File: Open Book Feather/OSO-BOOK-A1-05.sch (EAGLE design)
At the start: 129 parts, among them J1 SJ-43514-SMT, J2 10118193-0001LF, Q1 DMG341, Q2 IRLML0100, SW1 SPDT_SWITCH, U1 AP2112-3.3, U2 MCP73831T-2ACI/OT, U3 ATSAMD51J64-TQFP(10X10), U4 GD25Q16C (or GD25Q32C), U5 74AC165D, U6 GD25Q16C (or GD25Q32C), U7 MAX4468EKAT, X1 JSTPH, X2 2x5 0.05" SWD

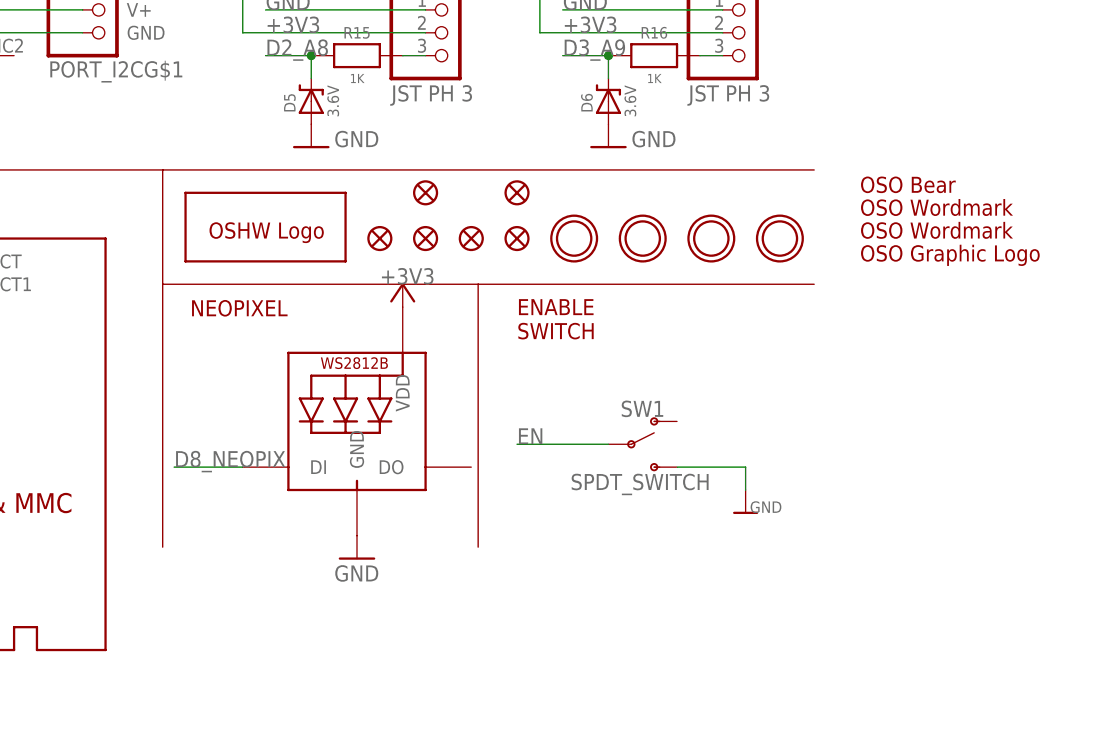
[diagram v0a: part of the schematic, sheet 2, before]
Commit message: right angle neopixel near reset button
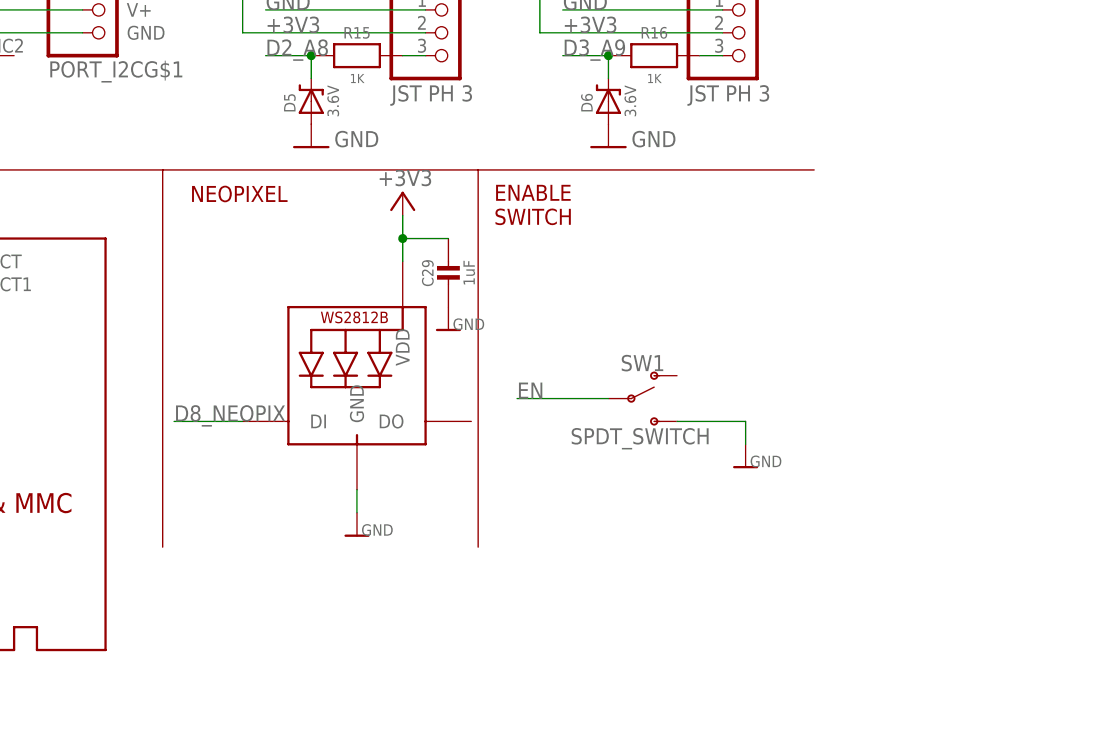
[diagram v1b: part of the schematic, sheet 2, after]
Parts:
- removed STATUS: WS2812B3535, adafruit:WS2812B3535
- added C36: 4.5nF, microbuilder:CAP_CERAMIC0805-NOOUTLINE
- added NEOPIX: WS2812B_4020, microbuilder:WS2812B_4020
- C29: value 4.5nF -> 1uF
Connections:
- net +3V3: now also C29.1, NEOPIX.VDD; no longer STATUS.VDD
- net D8_NEOPIX: now also NEOPIX.DI; no longer STATUS.DI
- net GND: now also C36.2, NEOPIX.GND; no longer STATUS.GND
- net SHIELD: now also C36.1; no longer C29.1
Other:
- moved on the sheet: SW1

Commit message: extend inductor's pad out from underneath
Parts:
- L1: device microbuilder:INDUCTORNR401 -> Adafruit 3.5in 480x320 FeatherWing:MICROBUILDER_INDUCTORNR401_BIGPADS
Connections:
- net +3V3: now also L1.1; no longer L1.2
- net N$3: now also L1.2; no longer L1.1
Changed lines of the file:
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@@
 <part name="C24" library="microbuilder" deviceset="CAP_CERAMIC" device="0805-NOOUTLINE" value="4.7uF/25V"/>
 <part name="D4" library="microbuilder" deviceset="DIODE-SCHOTTKY" device="SOD-123" value="MBR0530"/>
-<part name="L1" library="microbuilder" deviceset="INDUCTOR" device="NR401" value="10uH"/>
 <part name="R12" library="microbuilder" deviceset="RESISTOR" device="0805_10MGAP" value="0.47ohm"/>
 <part name="U$10" library="microbuilder" deviceset="GND" device=""/>
@@
 <part name="C29" library="microbuilder" deviceset="CAP_CERAMIC" device="0805-NOOUTLINE" value="1uF"/>
 <part name="U$46" library="microbuilder" deviceset="GND" device=""/>
+<part name="L1" library="Adafruit 3.5in 480x320 FeatherWing" deviceset="MICROBUILDER_INDUCTOR" device="NR401_BIGPADS" value="10uH"/>
 </parts>
 <sheets>
@@
 <attribute name="VALUE" x="104.1" y="144.78" size="1.27" layer="96" rot="MR270" align="center"/>
 </instance>
-<instance part="L1" gate="G$1" x="83.82" y="149.86" smashed="yes" rot="MR0">
-<attribute name="NAME" x="83.82" y="152.4" size="1.27" layer="95" rot="MR0" align="center"/>
-<attribute name="VALUE" x="83.82" y="148.32" size="1.27" layer="96" rot="MR0" align="center"/>
-</instance>
 <instance part="R12" gate="G$1" x="91.44" y="121.92" smashed="yes" rot="MR270">
 <attribute name="NAME" x="88.9" y="121.92" size="1.27" layer="95" font="vector" rot="MR270" align="center"/>
@@
 <instance part="U$46" gate="G$1" x="215.9" y="48.26" smashed="yes" rot="MR0">
 <attribute name="VALUE" x="219.964" y="48.26" size="1.27" layer="96" rot="MR0"/>
+</instance>
+<instance part="L1" gate="G$1" x="83.82" y="149.86" smashed="yes">
+<attribute name="NAME" x="83.82" y="152.4" size="1.27" layer="95" align="center"/>
+<attribute name="VALUE" x="83.82" y="148.32" size="1.27" layer="96" align="center"/>
 </instance>
 </instances>
@@
 <net name="+3V3" class="1">
 <segment>
-<pinref part="L1" gate="G$1" pin="2"/>
 <wire x1="76.2" y1="154.94" x2="76.2" y2="149.86" width="0.1524" layer="91"/>
 <wire x1="76.2" y1="149.86" x2="78.74" y2="149.86" width="0.1524" layer="91"/>
 <pinref part="+3V7" gate="G$1" pin="+3V3"/>
+<pinref part="L1" gate="G$1" pin="1"/>
 </segment>
 <segment>
@@
 <wire x1="91.44" y1="149.86" x2="101.6" y2="149.86" width="0.1524" layer="91"/>
 <wire x1="101.6" y1="149.86" x2="101.6" y2="147.32" width="0.1524" layer="91"/>
-<pinref part="L1" gate="G$1" pin="1"/>
 <wire x1="91.44" y1="149.86" x2="88.9" y2="149.86" width="0.1524" layer="91"/>
 <junction x="91.44" y="149.86"/>
@@
 <pinref part="C24" gate="G$1" pin="1"/>
 <wire x1="114.3" y1="149.86" x2="114.3" y2="144.78" width="0.1524" layer="91"/>
-</segment>
-</net>
+<pinref part="L1" gate="G$1" pin="2"/>
+</segment>
+</net>

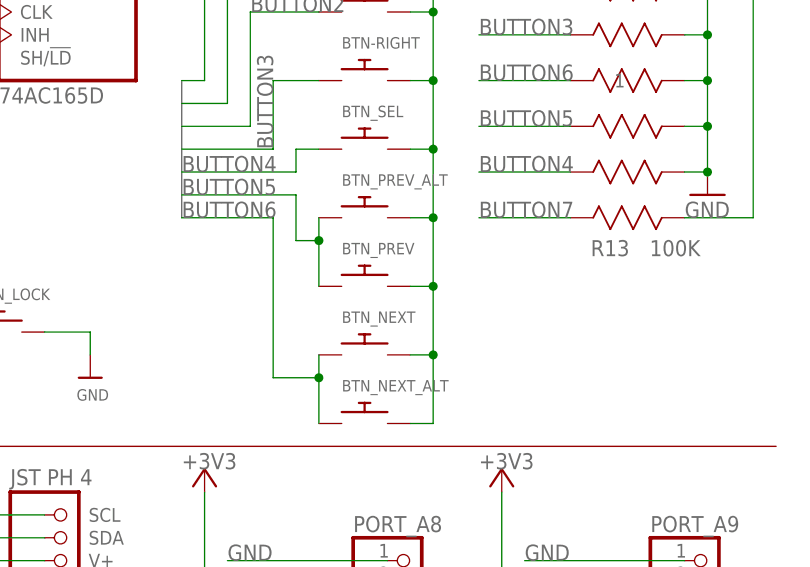
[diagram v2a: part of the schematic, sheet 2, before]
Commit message: DNP side buttons
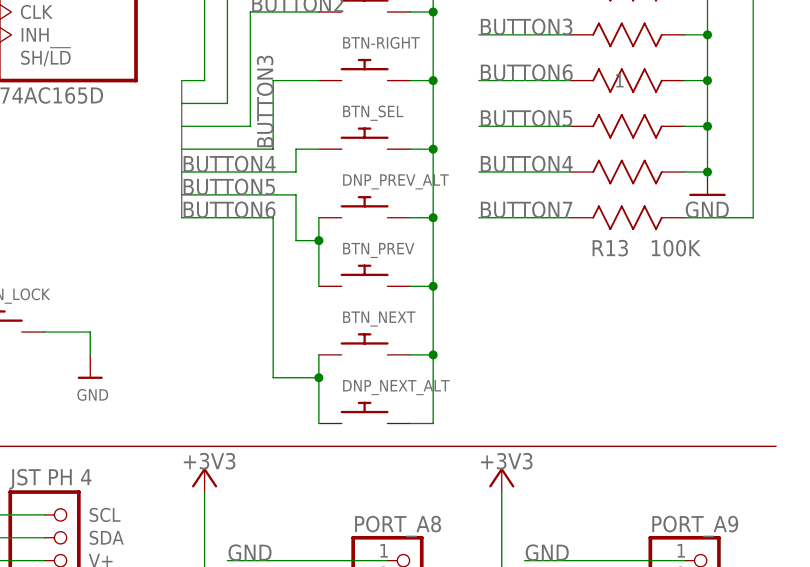
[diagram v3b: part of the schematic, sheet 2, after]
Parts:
- renumbered BTN_NEXT_ALT to DNP_NEXT_ALT, BTN_PREV_ALT to DNP_PREV_ALT

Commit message: last tweaks to A1-05 before sending to fab
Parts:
- removed U$44: OSO_GRAPHIC, My Stuff:OSO_GRAPHIC
- removed U$45: OSO_BEAR, My Stuff:OSO_BEAR
- removed U$47: OSO_TEXT, My Stuff:OSO_TEXT
- removed U$48: OSO_TEXTOSO_TEXT_ONELINE_125MIL, My Stuff:OSO_TEXTOSO_TEXT_ONELINE_125MIL
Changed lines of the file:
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@@
 <part name="GND7" library="supply1" deviceset="GND" device=""/>
 <part name="C10" library="microbuilder" deviceset="CAP_CERAMIC" device="0805_10MGAP" value="1uF"/>
-<part name="U$44" library="My Stuff" deviceset="OSO_GRAPHIC" device=""/>
-<part name="U$45" library="My Stuff" deviceset="OSO_BEAR" device=""/>
-<part name="U$47" library="My Stuff" deviceset="OSO_TEXT" device=""/>
-<part name="U$48" library="My Stuff" deviceset="OSO_TEXT" device="OSO_TEXT_ONELINE_125MIL"/>
 <part name="LED" library="adafruit" deviceset="LED" device="CHIP-LED0805" value="RED"/>
 <part name="CHG" library="adafruit" deviceset="LED" device="CHIP-LED0805" value="AMBER"/>
@@
 <instance part="FID5" gate="G$1" x="111.76" y="15.24" smashed="yes"/>
 <instance part="FID6" gate="G$1" x="121.92" y="15.24" smashed="yes"/>
-<instance part="U$44" gate="G$1" x="160.02" y="7.62" smashed="yes"/>
-<instance part="U$45" gate="G$1" x="160.02" y="15.24" smashed="yes"/>
-<instance part="U$47" gate="G$1" x="160.02" y="10.16" smashed="yes"/>
-<instance part="U$48" gate="G$1" x="160.02" y="12.7" smashed="yes"/>
 </instances>
 <busses>

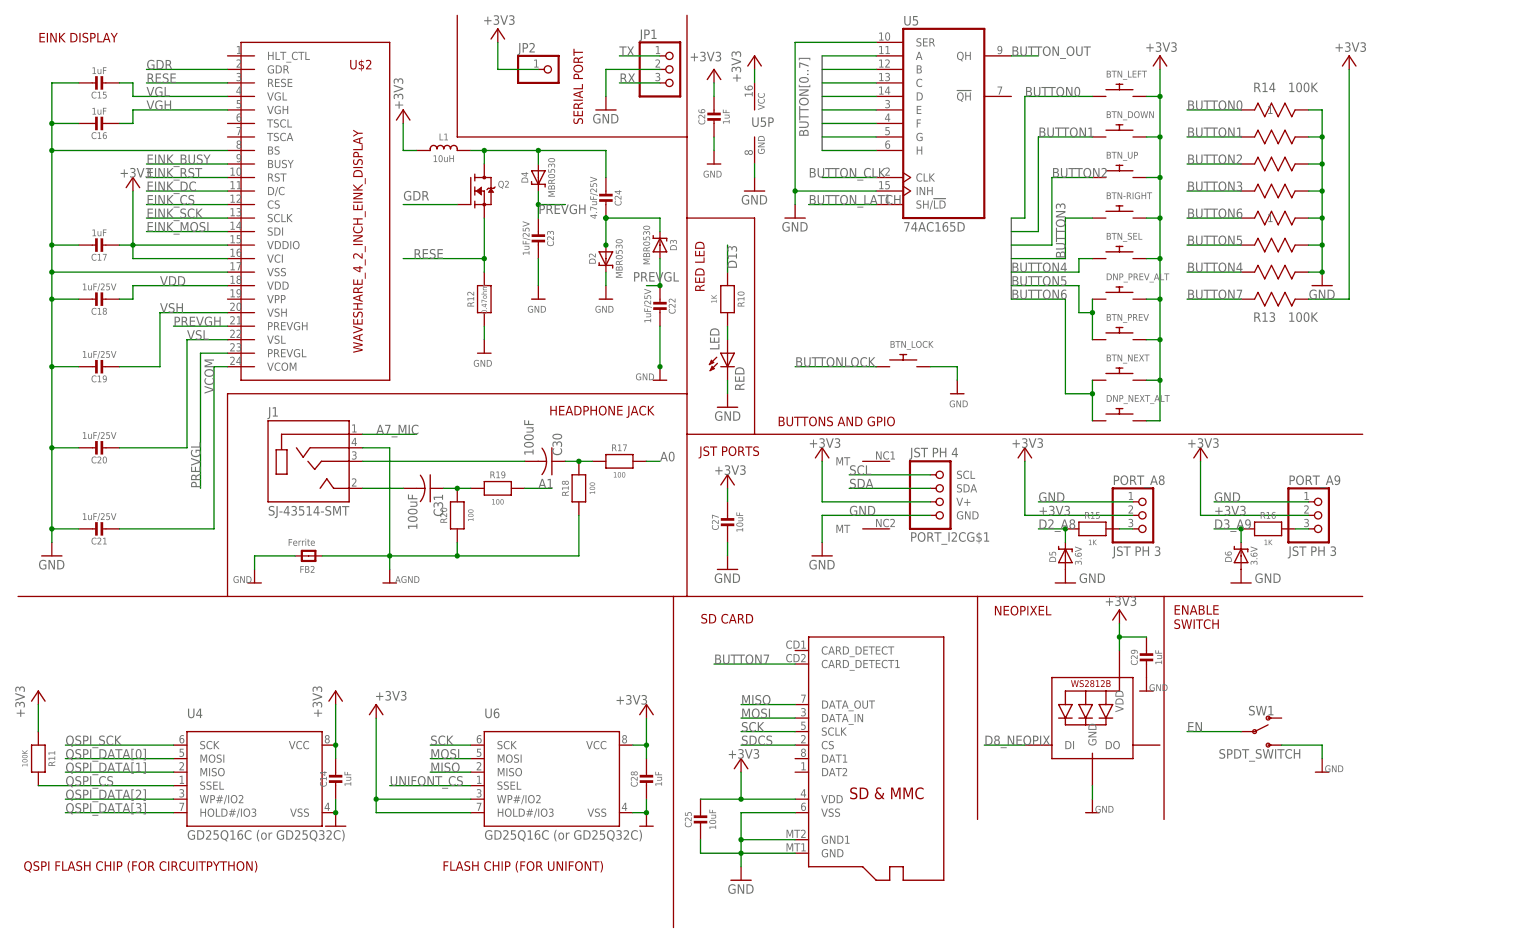
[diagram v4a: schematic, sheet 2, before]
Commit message: Buttons & SD card change
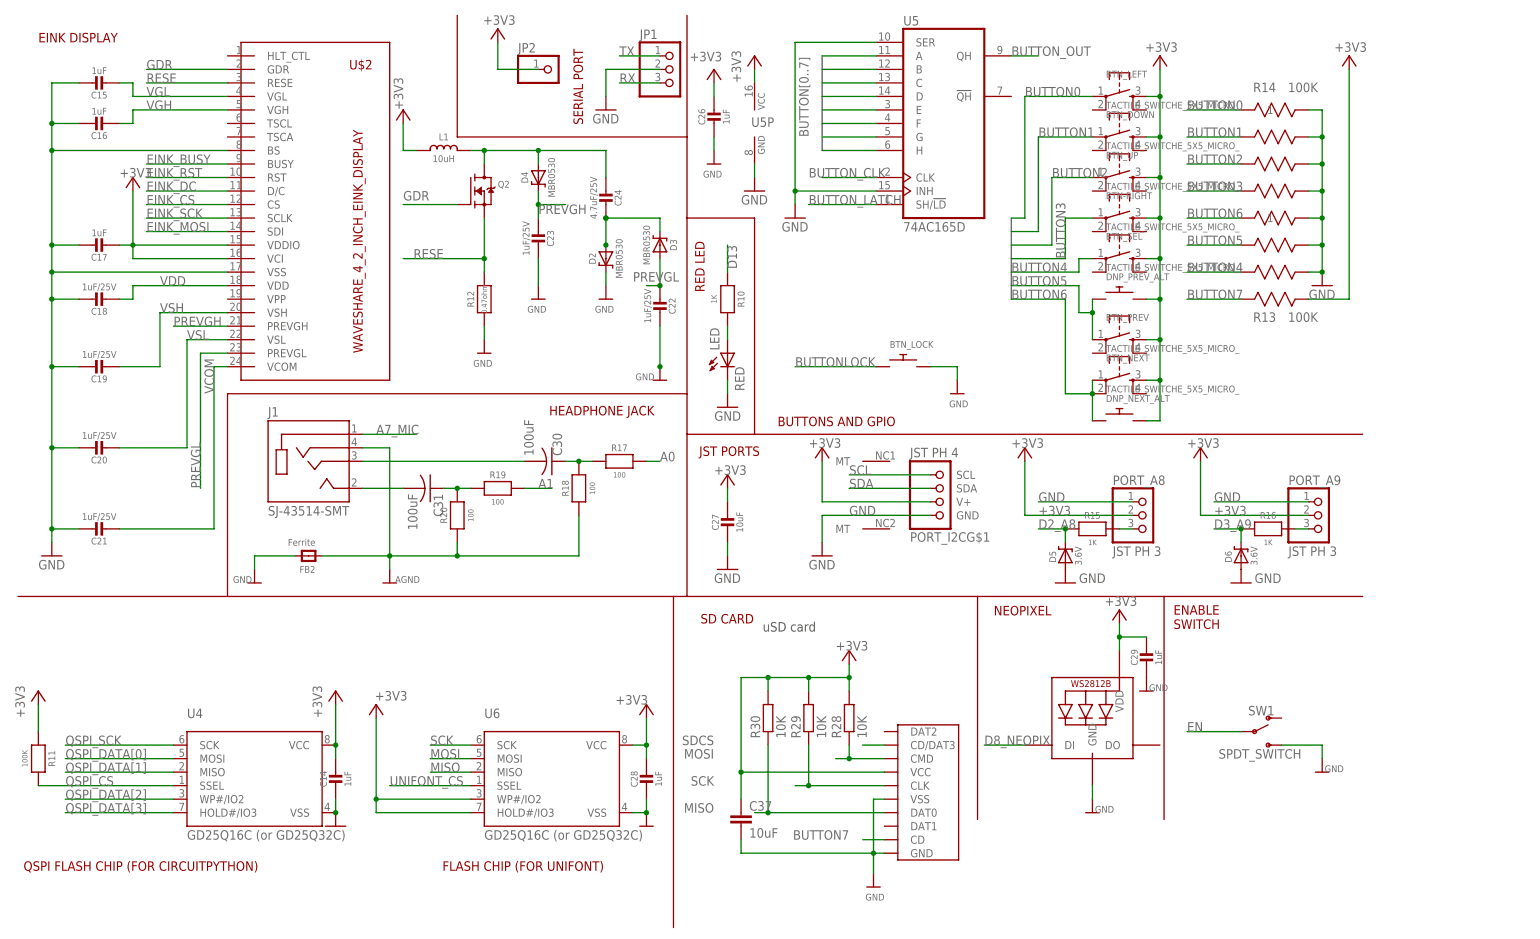
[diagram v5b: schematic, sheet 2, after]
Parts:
- removed C25: 10uF, microbuilder:CAP_CERAMIC0805_10MGAP
- removed MICROSD: MICROSD, adafruit:MICROSD
- added C37: 10uF, rcl:C-EUC0805
- added R28, R29, R30: 10K, rcl:R-EU_R0805
- added SD_CARD: MICRO_SD_CARD_, dronecz:MICRO_SD_CARD_
- BTN-RIGHT, BTN_DOWN, BTN_LEFT, BTN_NEXT, BTN_PREV, BTN_SEL, BTN_UP: value (none) -> TACTILE_SWITCHE_5X5_MICRO_; device adafruit:SWITCH_PUSHBUTTONEVQ-PE -> dronecz:TACTILE_SWITCHE_5X5_MICRO_
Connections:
- net +3V3: now also BTN-RIGHT.3, BTN_DOWN.3, BTN_LEFT.3, BTN_NEXT.3, BTN_PREV.3, BTN_SEL.3, BTN_UP.3, C37.1, R28.2, R29.2, R30.2, SD_CARD.VCC; no longer BTN-RIGHT.P$2, BTN_DOWN.P$2, BTN_LEFT.P$2, BTN_NEXT.P$2, BTN_PREV.P$2, BTN_SEL.P$2, BTN_UP.P$2, C25.1, MICROSD.VDD
- net BUTTON0: now also BTN_LEFT.1; no longer BTN_LEFT.P$1
- net BUTTON1: now also BTN_DOWN.1; no longer BTN_DOWN.P$1
- net BUTTON2: now also BTN_UP.1; no longer BTN_UP.P$1
- net BUTTON3: now also BTN-RIGHT.1; no longer BTN-RIGHT.P$1
- net BUTTON4: now also BTN_SEL.1; no longer BTN_SEL.P$1
- net BUTTON5: now also BTN_PREV.1; no longer BTN_PREV.P$1
- net BUTTON6: now also BTN_NEXT.1, BTN_NEXT.2; no longer BTN_NEXT.P$1
- net BUTTON7: now also SD_CARD.CD; no longer MICROSD.CARD_DETECT1
- net GND: now also C37.2, SD_CARD.GND, SD_CARD.VSS; no longer C25.2, MICROSD.GND, MICROSD.GND1, MICROSD.VSS
- net MISO: now also R30.1, SD_CARD.DAT0; no longer MICROSD.DATA_OUT
- net MOSI: now also R28.1, SD_CARD.CMD; no longer MICROSD.DATA_IN
- net SCK: now also R29.1, SD_CARD.CLK; no longer MICROSD.SCLK
- net SDCS: now also SD_CARD.CD/DAT3; no longer MICROSD.CS
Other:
- note added: "uSD card"

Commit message: Revert "Buttons & SD card change"
This reverts commit 564ec3b5048e0d7899cd32f6cb14d9a07736022d.
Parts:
- removed C37: 10uF, rcl:C-EUC0805
- removed R28, R29, R30: 10K, rcl:R-EU_R0805
- removed SD_CARD: MICRO_SD_CARD_, dronecz:MICRO_SD_CARD_
- added C25: 10uF, microbuilder:CAP_CERAMIC0805_10MGAP
- added MICROSD: MICROSD, adafruit:MICROSD
- BTN-RIGHT, BTN_DOWN, BTN_LEFT, BTN_NEXT, BTN_PREV, BTN_SEL, BTN_UP: value TACTILE_SWITCHE_5X5_MICRO_ -> (none); device dronecz:TACTILE_SWITCHE_5X5_MICRO_ -> adafruit:SWITCH_PUSHBUTTONEVQ-PE
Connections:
- net +3V3: now also BTN-RIGHT.P$2, BTN_DOWN.P$2, BTN_LEFT.P$2, BTN_NEXT.P$2, BTN_PREV.P$2, BTN_SEL.P$2, BTN_UP.P$2, C25.1, MICROSD.VDD; no longer BTN-RIGHT.3, BTN_DOWN.3, BTN_LEFT.3, BTN_NEXT.3, BTN_PREV.3, BTN_SEL.3, BTN_UP.3, C37.1, R28.2, R29.2, R30.2, SD_CARD.VCC
- net BUTTON0: now also BTN_LEFT.P$1; no longer BTN_LEFT.1
- net BUTTON1: now also BTN_DOWN.P$1; no longer BTN_DOWN.1
- net BUTTON2: now also BTN_UP.P$1; no longer BTN_UP.1
- net BUTTON3: now also BTN-RIGHT.P$1; no longer BTN-RIGHT.1
- net BUTTON4: now also BTN_SEL.P$1; no longer BTN_SEL.1
- net BUTTON5: now also BTN_PREV.P$1; no longer BTN_PREV.1
- net BUTTON6: now also BTN_NEXT.P$1; no longer BTN_NEXT.1, BTN_NEXT.2
- net BUTTON7: now also MICROSD.CARD_DETECT1; no longer SD_CARD.CD
- net GND: now also C25.2, MICROSD.GND, MICROSD.GND1, MICROSD.VSS; no longer C37.2, SD_CARD.GND, SD_CARD.VSS
- net MISO: now also MICROSD.DATA_OUT; no longer R30.1, SD_CARD.DAT0
- net MOSI: now also MICROSD.DATA_IN; no longer R28.1, SD_CARD.CMD
- net SCK: now also MICROSD.SCLK; no longer R29.1, SD_CARD.CLK
- net SDCS: now also MICROSD.CS; no longer SD_CARD.CD/DAT3
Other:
- note removed: "uSD card"
